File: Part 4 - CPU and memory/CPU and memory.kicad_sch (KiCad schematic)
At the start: 17 parts, among them U12 74AHC32, U13 74AHC32, U14 74AHC00, U15 74AHC174, U16 74AHC138, U17 Z80C0010, U18 SST39SF010, U19 AS6C4008

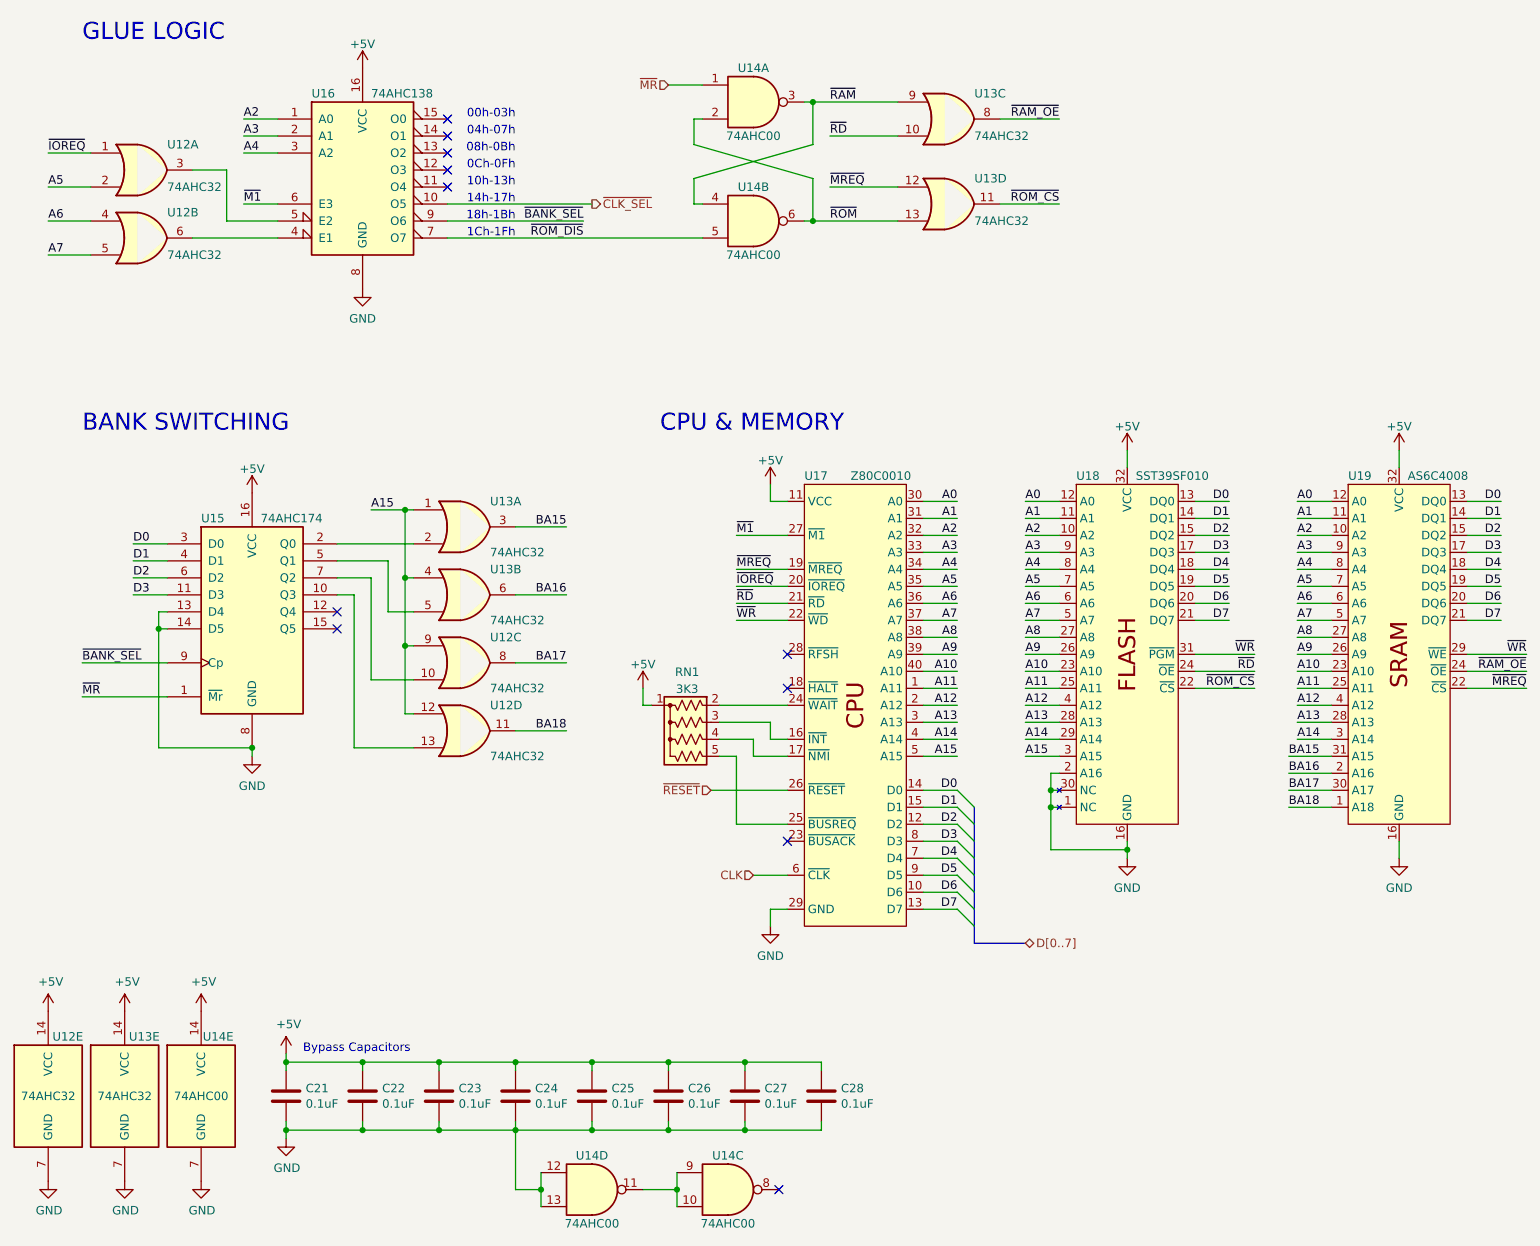
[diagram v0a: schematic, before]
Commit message: Backplane PCB sent out, and experimented with clock options
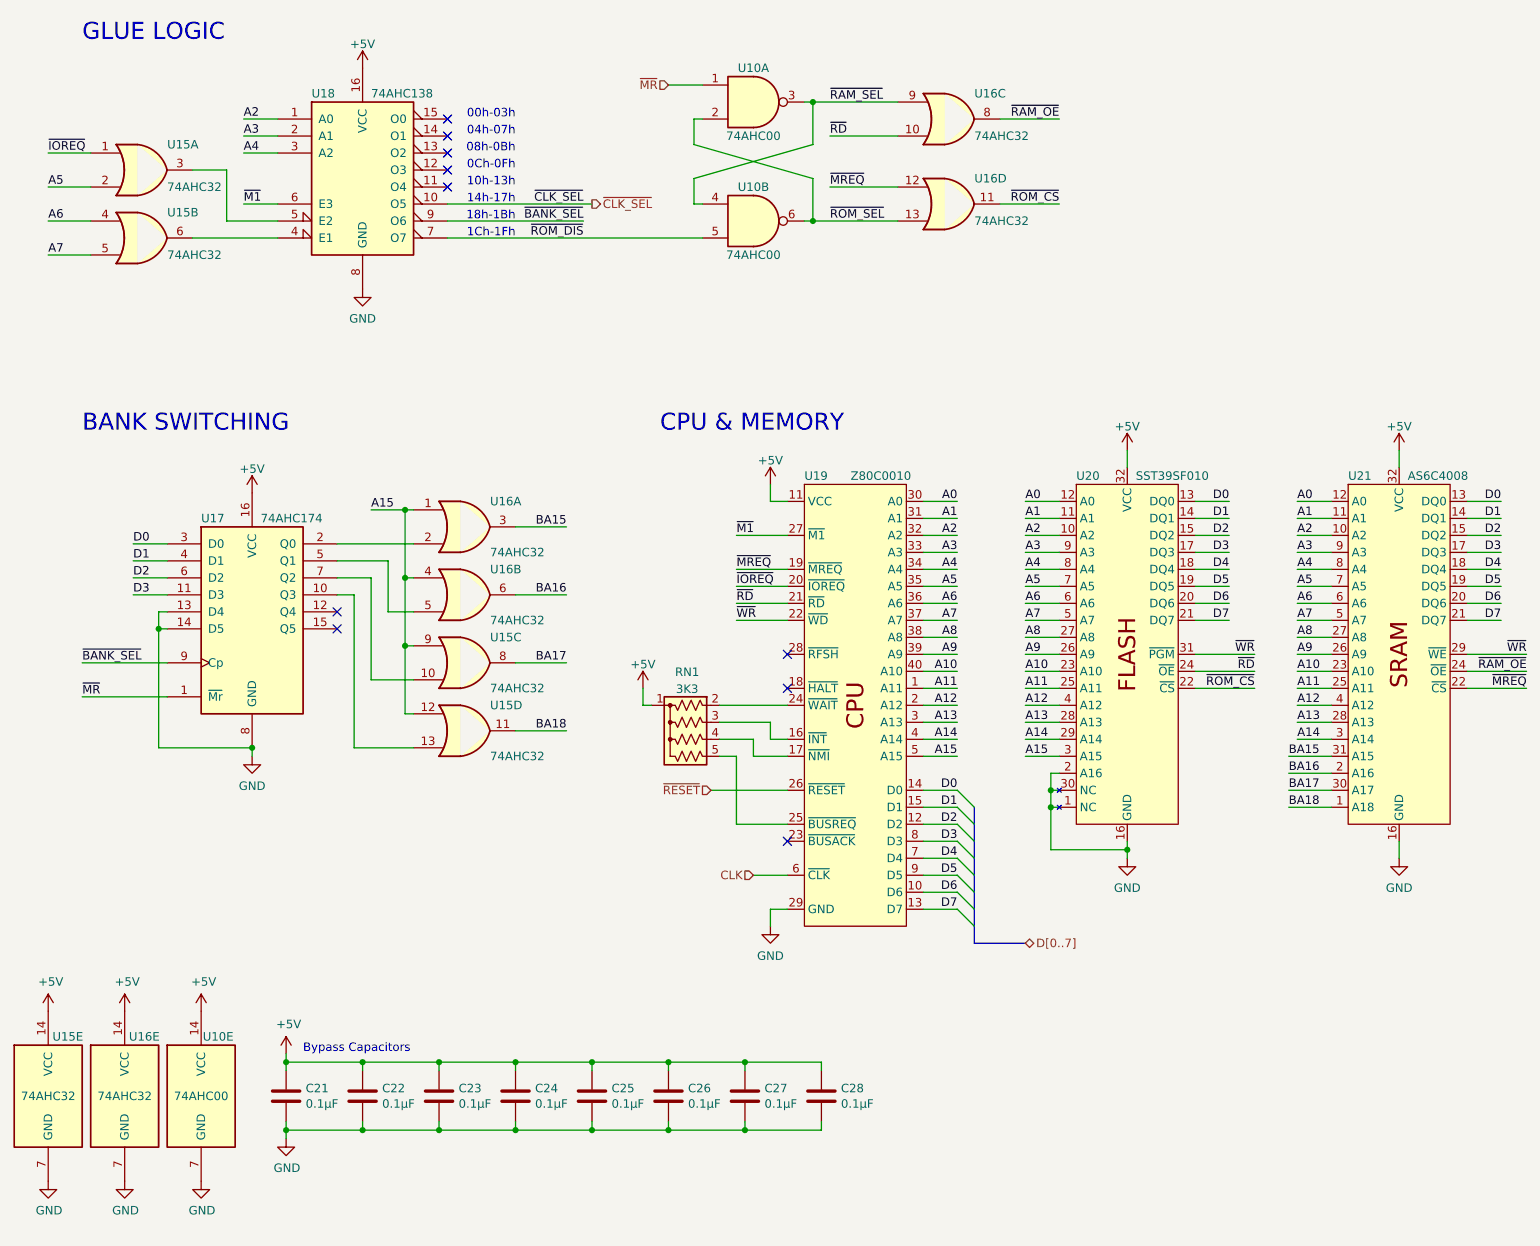
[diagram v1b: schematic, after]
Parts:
- removed unit 3 of U14
- removed unit 4 of U14
- C21, C22, C23, C24, C25, C26, C27, C28: value 0.1uF -> 0.1µF
- U15: renamed from U12; footprint Package_DIP:DIP-16_W7.62mm_Socket -> Package_DIP:DIP-14_W7.62mm_Socket
- U16: renamed from U13; footprint Package_DIP:DIP-16_W7.62mm_Socket -> Package_DIP:DIP-14_W7.62mm_Socket
- U17: renamed from U15; footprint Package_DIP:DIP-14_W7.62mm_Socket -> Package_DIP:DIP-16_W7.62mm_Socket
- U18: renamed from U16; footprint Package_DIP:DIP-14_W7.62mm_Socket -> Package_DIP:DIP-16_W7.62mm_Socket
- U19: renamed from U17; footprint Package_DIP:DIP-16_W7.62mm_Socket -> Package_DIP:DIP-40_W15.24mm_Socket
- U20: renamed from U18; footprint Package_DIP:DIP-16_W7.62mm_Socket -> Package_DIP:DIP-32_W15.24mm
- U21: renamed from U19; footprint Package_DIP:DIP-40_W15.24mm_Socket -> Package_DIP:DIP-32_W15.24mm
- renumbered U14 to U10
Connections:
- net ~{RAM} renamed ~{RAM_SEL}
- net ~{ROM} renamed ~{ROM_SEL}
- no-connect marks 11 -> 10
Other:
- company: Frédéric Segard -> Frederic Segard - aka: The Micro Hobbyist
